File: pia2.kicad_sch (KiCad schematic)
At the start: 41 parts, among them IC25 LM393P, IC31 74LS02N, IC34 MC14050BCP, IC35 MC6821

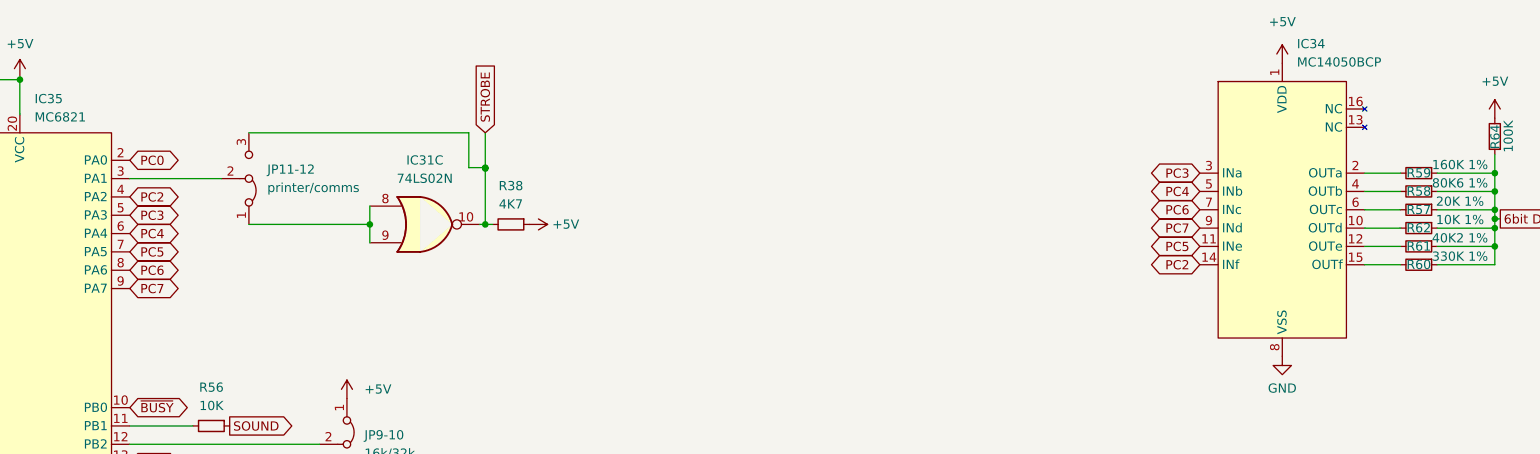
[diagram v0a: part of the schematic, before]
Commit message: improve annotation of dac
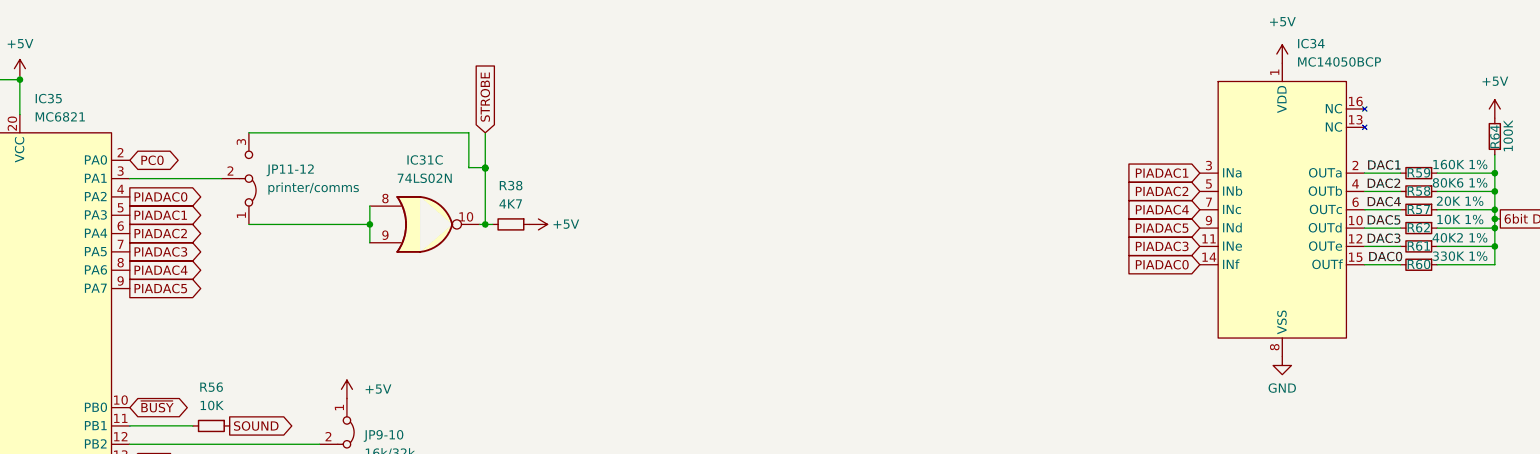
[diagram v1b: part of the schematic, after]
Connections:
- net DAC1: now reaches IC34.2 (OUTa), R59.2
- net DAC0: now reaches IC34.15 (OUTf), R60.2
- net DAC5: now reaches IC34.10 (OUTd), R62.2
- net DAC2: now reaches IC34.4 (OUTb), R58.2
- net DAC3: now reaches IC34.12 (OUTe), R61.2
- net DAC4: now reaches IC34.6 (OUTc), R57.2
- net PC2 renamed PIADAC0
- net PC3 renamed PIADAC1
- net PC4 renamed PIADAC2
- net PC5 renamed PIADAC3
- net PC6 renamed PIADAC4
- net PC7 renamed PIADAC5
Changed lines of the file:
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@@
     (stroke (width 0) (type default) (color 0 0 0 0))
   )
-  (global_label "PC3" (shape bidirectional) (at 74.93 45.212 0) (fields_autoplaced)
-    (effects (font (size 1.27 1.27)) (justify left))
-    (property "Intersheet References" "${INTERSHEET_REFS}" (id 0) (at 81.0037 45.1326 0)
+  (label "DAC3" (at 246.3611 49.53 0)
+    (effects (font (size 1.27 1.27)) (justify left bottom))
+  )
+  (label "DAC1" (at 246.4162 39.37 0)
+    (effects (font (size 1.27 1.27)) (justify left bottom))
+  )
+  (label "DAC5" (at 246.3611 46.99 0)
+    (effects (font (size 1.27 1.27)) (justify left bottom))
+  )
+  (label "DAC4" (at 246.3611 44.45 0)
+    (effects (font (size 1.27 1.27)) (justify left bottom))
+  )
+  (label "DAC2" (at 246.3611 41.91 0)
+    (effects (font (size 1.27 1.27)) (justify left bottom))
+  )
+  (label "DAC0" (at 246.5816 52.07 0)
+    (effects (font (size 1.27 1.27)) (justify left bottom))
+  )
+  (global_label "PIADAC1" (shape output) (at 74.93 45.212 0) (fields_autoplaced)
+    (effects (font (size 1.27 1.27)) (justify left))
+    (property "Intersheet References" "${INTERSHEET_REFS}" (id 0) (at 85.0556 45.1326 0)
       (effects (font (size 1.27 1.27)) (justify left) hide)
     )
@@
     )
   )
-  (global_label "PC6" (shape bidirectional) (at 74.93 52.832 0) (fields_autoplaced)
-    (effects (font (size 1.27 1.27)) (justify left))
-    (property "Intersheet References" "${INTERSHEET_REFS}" (id 0) (at 81.0037 52.7526 0)
+  (global_label "PIADAC4" (shape output) (at 74.93 52.832 0) (fields_autoplaced)
+    (effects (font (size 1.27 1.27)) (justify left))
+    (property "Intersheet References" "${INTERSHEET_REFS}" (id 0) (at 85.0556 52.7526 0)
       (effects (font (size 1.27 1.27)) (justify left) hide)
     )
@@
     )
   )
-  (global_label "PC4" (shape bidirectional) (at 74.93 47.752 0) (fields_autoplaced)
-    (effects (font (size 1.27 1.27)) (justify left))
-    (property "Intersheet References" "${INTERSHEET_REFS}" (id 0) (at 81.0037 47.6726 0)
+  (global_label "PIADAC2" (shape output) (at 74.93 47.752 0) (fields_autoplaced)
+    (effects (font (size 1.27 1.27)) (justify left))
+    (property "Intersheet References" "${INTERSHEET_REFS}" (id 0) (at 85.0556 47.6726 0)
       (effects (font (size 1.27 1.27)) (justify left) hide)
     )
@@
     )
   )
-  (global_label "PC4" (shape bidirectional) (at 223.266 41.91 180) (fields_autoplaced)
-    (effects (font (size 1.27 1.27)) (justify right))
-    (property "Intersheet References" "${INTERSHEET_REFS}" (id 0) (at 217.1923 41.8306 0)
+  (global_label "PIADAC2" (shape input) (at 223.266 41.91 180) (fields_autoplaced)
+    (effects (font (size 1.27 1.27)) (justify right))
+    (property "Intersheet References" "${INTERSHEET_REFS}" (id 0) (at 213.1404 41.8306 0)
       (effects (font (size 1.27 1.27)) (justify right) hide)
     )
@@
     )
   )
-  (global_label "PC6" (shape bidirectional) (at 223.266 44.45 180) (fields_autoplaced)
-    (effects (font (size 1.27 1.27)) (justify right))
-    (property "Intersheet References" "${INTERSHEET_REFS}" (id 0) (at 217.1923 44.3706 0)
+  (global_label "PIADAC4" (shape input) (at 223.266 44.45 180) (fields_autoplaced)
+    (effects (font (size 1.27 1.27)) (justify right))
+    (property "Intersheet References" "${INTERSHEET_REFS}" (id 0) (at 213.1404 44.3706 0)
       (effects (font (size 1.27 1.27)) (justify right) hide)
     )
@@
     )
   )
-  (global_label "PC7" (shape bidirectional) (at 223.266 46.99 180) (fields_autoplaced)
-    (effects (font (size 1.27 1.27)) (justify right))
-    (property "Intersheet References" "${INTERSHEET_REFS}" (id 0) (at 217.1923 46.9106 0)
+  (global_label "PIADAC5" (shape input) (at 223.266 46.99 180) (fields_autoplaced)
+    (effects (font (size 1.27 1.27)) (justify right))
+    (property "Intersheet References" "${INTERSHEET_REFS}" (id 0) (at 213.1404 46.9106 0)
       (effects (font (size 1.27 1.27)) (justify right) hide)
     )
@@
     )
   )
-  (global_label "PC2" (shape bidirectional) (at 223.266 52.07 180) (fields_autoplaced)
-    (effects (font (size 1.27 1.27)) (justify right))
-    (property "Intersheet References" "${INTERSHEET_REFS}" (id 0) (at 217.1923 51.9906 0)
+  (global_label "PIADAC0" (shape input) (at 223.266 52.07 180) (fields_autoplaced)
+    (effects (font (size 1.27 1.27)) (justify right))
+    (property "Intersheet References" "${INTERSHEET_REFS}" (id 0) (at 213.1404 51.9906 0)
       (effects (font (size 1.27 1.27)) (justify right) hide)
     )
@@
     )
   )
-  (global_label "PC3" (shape bidirectional) (at 223.266 39.37 180) (fields_autoplaced)
-    (effects (font (size 1.27 1.27)) (justify right))
-    (property "Intersheet References" "${INTERSHEET_REFS}" (id 0) (at 217.1923 39.2906 0)
-      (effects (font (size 1.27 1.27)) (justify right) hide)
-    )
-  )
-  (global_label "PC2" (shape bidirectional) (at 74.93 42.672 0) (fields_autoplaced)
-    (effects (font (size 1.27 1.27)) (justify left))
-    (property "Intersheet References" "${INTERSHEET_REFS}" (id 0) (at 81.0037 42.5926 0)
+  (global_label "PIADAC1" (shape input) (at 223.266 39.37 180) (fields_autoplaced)
+    (effects (font (size 1.27 1.27)) (justify right))
+    (property "Intersheet References" "${INTERSHEET_REFS}" (id 0) (at 213.1404 39.2906 0)
+      (effects (font (size 1.27 1.27)) (justify right) hide)
+    )
+  )
+  (global_label "PIADAC0" (shape output) (at 74.93 42.672 0) (fields_autoplaced)
+    (effects (font (size 1.27 1.27)) (justify left))
+    (property "Intersheet References" "${INTERSHEET_REFS}" (id 0) (at 85.0556 42.5926 0)
       (effects (font (size 1.27 1.27)) (justify left) hide)
     )
@@
     )
   )
-  (global_label "PC5" (shape bidirectional) (at 74.93 50.292 0) (fields_autoplaced)
-    (effects (font (size 1.27 1.27)) (justify left))
-    (property "Intersheet References" "${INTERSHEET_REFS}" (id 0) (at 81.0037 50.2126 0)
+  (global_label "PIADAC3" (shape output) (at 74.93 50.292 0) (fields_autoplaced)
+    (effects (font (size 1.27 1.27)) (justify left))
+    (property "Intersheet References" "${INTERSHEET_REFS}" (id 0) (at 85.0556 50.2126 0)
       (effects (font (size 1.27 1.27)) (justify left) hide)
     )
@@
     )
   )
-  (global_label "PC7" (shape bidirectional) (at 74.93 55.372 0) (fields_autoplaced)
-    (effects (font (size 1.27 1.27)) (justify left))
-    (property "Intersheet References" "${INTERSHEET_REFS}" (id 0) (at 81.0037 55.2926 0)
+  (global_label "PIADAC5" (shape output) (at 74.93 55.372 0) (fields_autoplaced)
+    (effects (font (size 1.27 1.27)) (justify left))
+    (property "Intersheet References" "${INTERSHEET_REFS}" (id 0) (at 85.0556 55.2926 0)
       (effects (font (size 1.27 1.27)) (justify left) hide)
     )
@@
     )
   )
-  (global_label "PC5" (shape bidirectional) (at 223.266 49.53 180) (fields_autoplaced)
-    (effects (font (size 1.27 1.27)) (justify right))
-    (property "Intersheet References" "${INTERSHEET_REFS}" (id 0) (at 217.1923 49.4506 0)
-      (effects (font (size 1.27 1.27)) (justify right) hide)
-    )
+  (global_label "PIADAC3" (shape input) (at 223.266 49.53 180) (fields_autoplaced)
+    (effects (font (size 1.27 1.27)) (justify right))
+    (property "Intersheet References" "${INTERSHEET_REFS}" (id 0) (at 213.1404 49.4506 0)
+      (effects (font (size 1.27 1.27)) (justify right) hide)
+    )

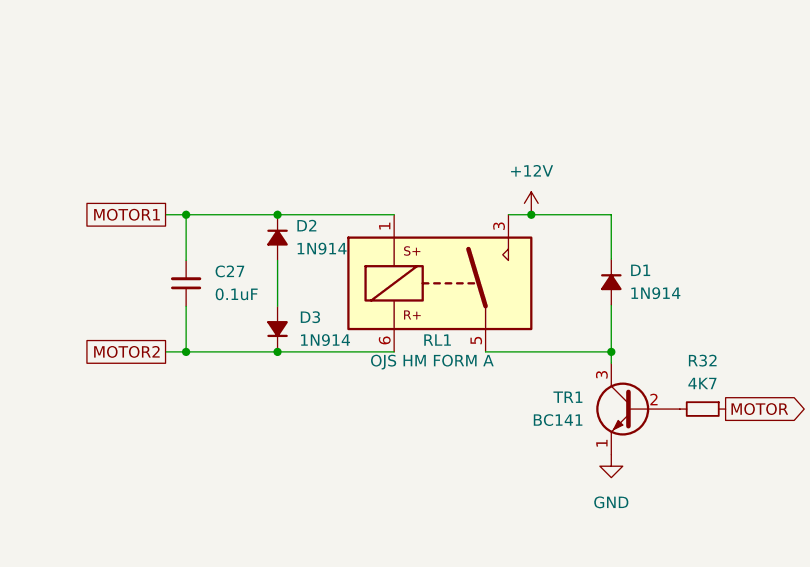
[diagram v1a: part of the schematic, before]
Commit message: rewire relay position
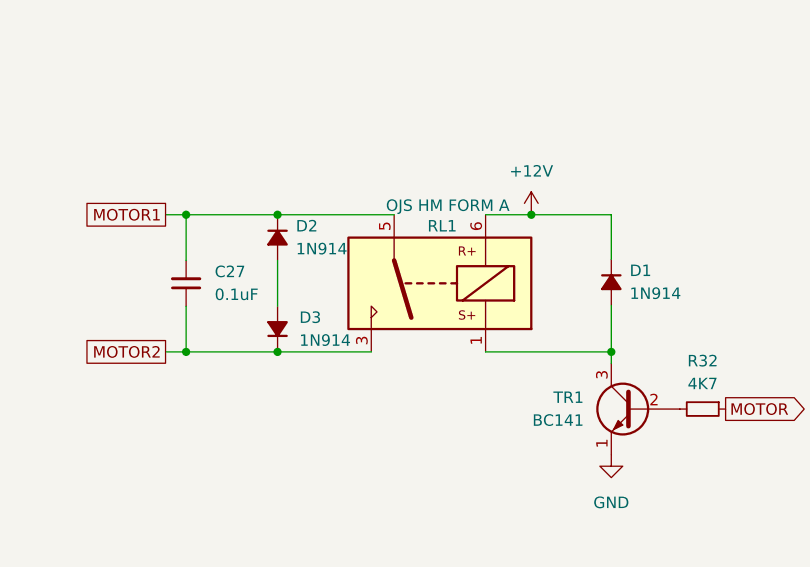
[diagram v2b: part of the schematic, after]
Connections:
- net +12V: now also RL1.6; no longer RL1.3
- net MOTOR1: now also RL1.5; no longer RL1.1
- net MOTOR2: now also RL1.3; no longer RL1.6
- net at D1.2 (A), TR1.3 (C): now also RL1.1; no longer RL1.5
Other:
- moved on the sheet: RL1
